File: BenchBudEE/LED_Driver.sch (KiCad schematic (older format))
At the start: 6 parts, among them U5 AP5726

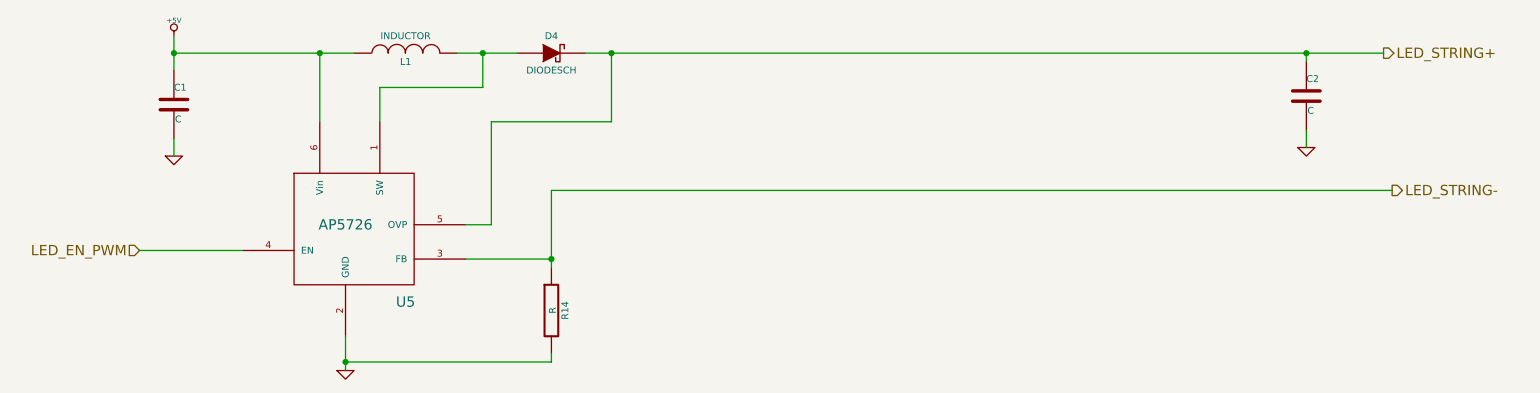
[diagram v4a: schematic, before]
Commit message: Associating and Placing the LED Driver Module
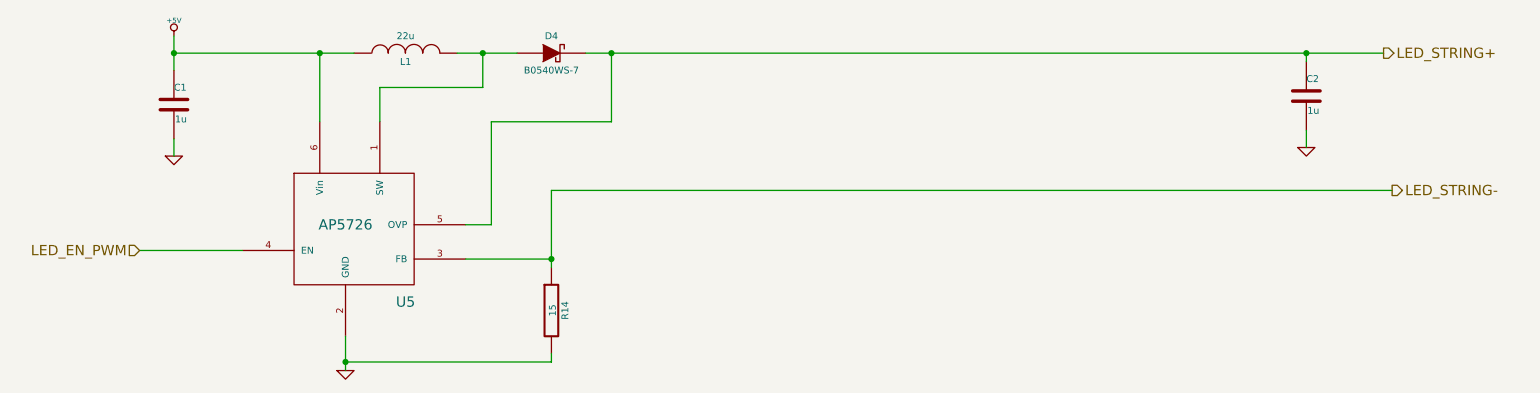
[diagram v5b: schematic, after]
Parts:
- C1, C2: value C -> 1u
- D4: value DIODESCH -> B0540WS-7
- L1: value INDUCTOR -> 22u; MFG Part Number (none) -> NR4012T220M
- R14: value R -> 15
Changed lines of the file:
@@
 Sheet 3 9
 Title ""
-Date "23 feb 2014"
+Date "27 feb 2014"
 Rev ""
 Comp ""
@@
 P 2250 1450
 F 0 "C1" H 2250 1550 40  0000 L CNN
-F 1 "C" H 2256 1365 40  0000 L CNN
+F 1 "1u" H 2256 1365 40  0000 L CNN
 F 2 "~" H 2288 1300 30  0000 C CNN
 F 3 "~" H 2250 1450 60  0000 C CNN
@@
 P 3600 1150
 F 0 "L1" V 3550 1150 40  0000 C CNN
-F 1 "INDUCTOR" V 3700 1150 40  0000 C CNN
+F 1 "22u" V 3700 1150 40  0000 C CNN
 F 2 "~" H 3600 1150 60  0000 C CNN
 F 3 "~" H 3600 1150 60  0000 C CNN
+F 4 "NR4012T220M" H 3600 1150 60  0001 C CNN "MFG Part Number"
 	1    3600 1150
 	0    -1   -1   0
@@
 P 8850 1400
 F 0 "C2" H 8850 1500 40  0000 L CNN
-F 1 "C" H 8856 1315 40  0000 L CNN
+F 1 "1u" H 8856 1315 40  0000 L CNN
 F 2 "~" H 8888 1250 30  0000 C CNN
 F 3 "~" H 8850 1400 60  0000 C CNN
@@
 P 4450 1150
 F 0 "D4" H 4450 1250 40  0000 C CNN
-F 1 "DIODESCH" H 4450 1050 40  0000 C CNN
+F 1 " B0540WS-7" H 4450 1050 40  0000 C CNN
 F 2 "~" H 4450 1150 60  0000 C CNN
 F 3 "~" H 4450 1150 60  0000 C CNN
@@
 P 4450 2650
 F 0 "R14" V 4530 2650 40  0000 C CNN
-F 1 "R" V 4457 2651 40  0000 C CNN
+F 1 "15" V 4457 2651 40  0000 C CNN
 F 2 "~" V 4380 2650 30  0000 C CNN
 F 3 "~" H 4450 2650 30  0000 C CNN

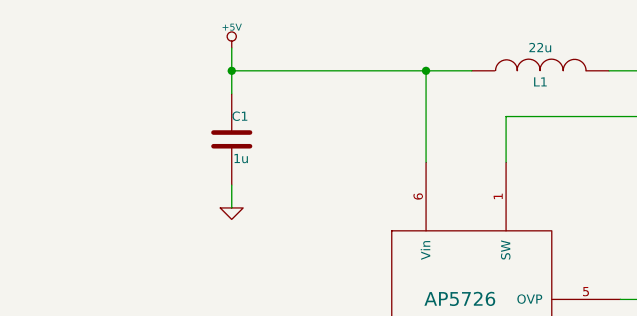
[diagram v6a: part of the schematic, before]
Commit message: Ground and Power Planes
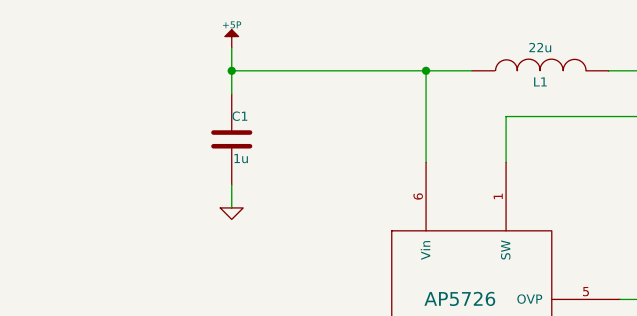
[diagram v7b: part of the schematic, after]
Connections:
- net +5V renamed +5P
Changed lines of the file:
@@
 Sheet 3 9
 Title ""
-Date "27 feb 2014"
+Date "1 mar 2014"
 Rev ""
 Comp ""
@@
 $EndComp
 $Comp
-L +5V #PWR018
-U 1 1 52F7B180
-P 2250 1050
-F 0 "#PWR018" H 2250 1140 20  0001 C CNN
-F 1 "+5V" H 2250 1140 30  0000 C CNN
-F 2 "" H 2250 1050 60  0000 C CNN
-F 3 "" H 2250 1050 60  0000 C CNN
-	1    2250 1050
-	1    0    0    -1
-$EndComp
-$Comp
-L GND #PWR019
+L GND #PWR19
 U 1 1 52F7B18F
 P 2250 1750
-F 0 "#PWR019" H 2250 1750 30  0001 C CNN
+F 0 "#PWR19" H 2250 1750 30  0001 C CNN
 F 1 "GND" H 2250 1680 30  0001 C CNN
 F 2 "" H 2250 1750 60  0000 C CNN
@@
 $EndComp
 $Comp
-L GND #PWR020
+L GND #PWR20
 U 1 1 52F7B19C
 P 3250 3000
-F 0 "#PWR020" H 3250 3000 30  0001 C CNN
+F 0 "#PWR20" H 3250 3000 30  0001 C CNN
 F 1 "GND" H 3250 2930 30  0001 C CNN
 F 2 "" H 3250 3000 60  0000 C CNN
@@
 Connection ~ 4050 1150
 $Comp
-L GND #PWR021
+L GND #PWR21
 U 1 1 52F7B218
 P 8850 1700
-F 0 "#PWR021" H 8850 1700 30  0001 C CNN
+F 0 "#PWR21" H 8850 1700 30  0001 C CNN
 F 1 "GND" H 8850 1630 30  0001 C CNN
 F 2 "" H 8850 1700 60  0000 C CNN
@@
 	9350 1950 4450 1950
 Connection ~ 4450 2350
+$Comp
+L +5P #PWR18
+U 1 1 5311DB16
+P 2250 1050
+F 0 "#PWR18" H 2250 1180 20  0001 C CNN
+F 1 "+5P" H 2250 1150 30  0000 C CNN
+F 2 "" H 2250 1050 60  0000 C CNN
+F 3 "" H 2250 1050 60  0000 C CNN
+	1    2250 1050
+	1    0    0    -1
+$EndComp
 $EndSCHEMATC
